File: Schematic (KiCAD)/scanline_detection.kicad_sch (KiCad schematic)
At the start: 95 parts, among them M2 NOR_2, M3 BIGBUF, X12 D-FF Reset, X13 NAND_2, X14 BUFFER, X16 INVERT, X17 NAND_2, X26 INVERT, X27 D-FF No Reset, X28 INVERT, X4 NAND_2, X5 D-FF No Reset, X6 NAND_4, X7 INVERT, X8 Reg 2 DFF-No-Reset N, X9 NAND_2, Y1 BUFFER, Y10 XNOR_2, Y13 XNOR_2, Y15 NOR_2, Y17 XNOR_2, Y2,7,9,14,16,21,23,28 Reg 8 D-Latch, Y20 XNOR_2, Y22 NAND_4, Y24 XNOR_2, Y27 XNOR_2, Y29 NOR_2, Y3 XNOR_2, Y30 INVERT, Y31 D-FF Reset, Y32 INVERT, Y6 XNOR_2, Y8 NAND_4

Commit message: - Lots of additional comments and signal name improvements.  - "Don't know what this is yet but it is important" section of the pulse channels:    - I worked out the logic and it is a 4-bit binary up-counter with preload, made from gates and D-latches instead of T-flip-flops.    - It is extremely similar to the envelope counter, but takes twice the die space and much more traces.    - None of its outputs go anywhere else, so I believe that it has no actual function.    - It seems to be a previous attempt at making the envelope counter and it got disconnected and left in.    - Each pulse channel has its own copy and I moved both of them to the "Artifacts" sheet.    - The wasted space amounts to about half of one of the large columns on the left side of the die.  - A couple of "OAI2" cells that noted "unclear order": I determined the correct order of the inputs based on several others which were known.  - Deduced the purpose of the 2 separate methods of scanline detection:    - The one looking for 3 consecutive reads finds the start of a scanline.    - The one counting PPU /RD to find PPU cycle 336, finds the end of the scanline.    - I moved these beside each other on the same sheet for clarity.  - A66.5 Changed from Nand to Nor in order to make sense.  - Basic test mode:    - Pin 92: Active low, enables test mode.    - Pin 29: In test mode, it gives external control of "Scanline Start Detection", which is normally done with the familiar 3 matching PPU reads.  When not in test mode, the pin has no function.    - Pin 30: In test mode, it gives external control of "Scanline End Detection", which is normally done by counting PPU /RD to find PPU cycle 336.  It also gives control of "Pulse Length Clock" when in test mode.  When not in test mode, the pin has no function.    - Pin 98/SL3: In test mode, it gives external control of "Pulse Timer Clock".  Whether or not in test mode, this pin low makes the MMC5 pretend $5104 had not yet been written since reset, probably as a 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
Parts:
- added P3, P4, R7, R8: INVERT, symbol MMC5:INVERT
- added R1: AOI_2, symbol MMC5:AOI_2
- added R6: NAND_2, symbol MMC5:NAND_2
- added T5: BUFFER, symbol MMC5:BUFFER
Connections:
- net External_Scanline_Input_PIN_29 is gone; now on net /Test_Input_PIN_29{PinInv}: AA4. (X)
- net at X7. (X): now also Z23. (/Q); no longer X6. (X)
- net at X13. (X): now also X12. (/Q); no longer X14. (X)
- net at X9. (X): now also Z24. (X); no longer X8. (/Q1)
- net at AA10. (X): now also AA13. (X); no longer AA9. (X)
- net at AA16. (X): now also AA14. (X); no longer AA17. (X)
- net at Z2-Z18. (/Q7): now also Y3. (X); no longer Z19. (X)
- net at Y29. (X): now also Y31. (/Q); no longer Y30. (X)
- net at Y15. (X): now also Y22. (X); no longer Y29. (X)
- net /Scanline_Start_Detected{AA3}: now reaches Y31. (/Q)
- net /Scanline_Start_Detected{AA3}: now also AA3. (X), R2. (X), Z1. (X), Z23. (/Q); no longer Y29. (X)
- net at Y17. (X): now also Y22. (X); no longer Y2,7,9,14,16,21,23,28. (Q7)
- net at Y24. (X): now also Y22. (X); no longer Y2,7,9,14,16,21,23,28. (Q7)
- net at Y20. (X): now also Y22. (X); no longer Y2,7,9,14,16,21,23,28. (Q7)
- net at Y6. (X): now also Y8. (X); no longer Y2,7,9,14,16,21,23,28. (Q7)
- net at Y13. (X): now also Y8. (X); no longer Y2,7,9,14,16,21,23,28. (Q7)
- net at Y10. (X): now also Y8. (X); no longer Y2,7,9,14,16,21,23,28. (Q7)
- net at Y3. (X): now also Y8. (X); no longer Y2,7,9,14,16,21,23,28. (Q7)
- net at Y27. (X): now also Y22. (X); no longer Y2,7,9,14,16,21,23,28. (Q7)
- net at AA20. (X): now also AA16. (X); no longer AA21. (X)
- net at AA19. (X): now also AB18. (X); no longer AA22. (X)
- net at AA15. (X): now also AB17. (X); no longer AA11. (X)
- net at X17. (X): now also Z20. (X); no longer X26. (X)
- net at Y8. (X): now also Y15. (X); no longer Y6. (X)
- net at AA5. (X): now also AA15. (X); no longer AA10. (X)
- net at AA2. (X): now also AB1. (X); no longer AA3. (X)
- net /Test_Input_PIN_29{PinInv}: now reaches AA4. (X)
- net /Test_Input_PIN_29{PinInv}: no longer AA2. (X)
- net at AB1. (X): now also AB2(a). (X); no longer AA2. (X)
- net at N39. (X): now also N38. (X); no longer M2. (X)
- net +Use_Internal_Scanline_Detection_PIN_92 renamed +Test_Mode_PIN_92{PinInv}
- removed net +Use_Internal_Scanline_Detection{AA1}: AA1. (X), AA2. (X)
- removed net /New_Scanline_Detected{AA3}: AA3. (X), R2. (X), Y31. (/Q), Z1. (X), Z23. (/Q)
- net /New_Scanline_Detected{R2} renamed /Scanline_Start_Detected{R2}
- removed net /Use_Internal_Scanline_Detection{AA1}: AA1. (X), AA2. (X)
- new net: X4. (X), X5. (/Q)
- new net: X16. (X), X4. (X)
- new net: X5. (/Q), X6. (X)
- new net: X6. (X), X7. (X)
- new net: X13. (X), X14. (X)
- new net: X13. (X), Y31. (/Q), Y32. (X)
- new net: P4. (X), R1. (X)
- new net: AA1. (X), AA2. (X), R1. (X) (x2)
- new net: P3. (X), R1. (X)
- new net: X8. (/Q1), X9. (X) (x2)
- new net: AA9. (X), AB6. (/Q)
- new net: AA10. (X), AA9. (X)
- new net: AA17. (X), AB16. (/Q)
- new net: AA16. (X), AA17. (X)
- new net: Z19. (X), Z2-Z18. (/Q7)
- new net: R6. (X), R7. (X)
- new net: Y29. (X), Y30. (X)
- new net: Y15. (X), Y29. (X)
- new net: Y1. (X), Y2,7,9,14,16,21,23,28. (Q7)
- new net: Y17. (X), Y2,7,9,14,16,21,23,28. (Q7)
- new net: Y2,7,9,14,16,21,23,28. (Q7), Y24. (X)
- new net: Y2,7,9,14,16,21,23,28. (Q7), Y20. (X)
- new net: Y2,7,9,14,16,21,23,28. (Q7), Y6. (X)
- new net: Y13. (X), Y2,7,9,14,16,21,23,28. (Q7)
- new net: Y10. (X), Y2,7,9,14,16,21,23,28. (Q7)
- new net: Y2,7,9,14,16,21,23,28. (Q7), Y3. (X)
- new net: Y2,7,9,14,16,21,23,28. (Q7), Y27. (X)
- new net: AA20. (X), AA21. (X)
- new net: AA21. (X), AB22. (/Q)
- new net: AA7. (X), AB10. (/Q), AB13. (/Q), AB16. (/Q), AB19. (/Q), AB22. (/Q), AB6. (/Q), AB7. (/Q)
- new net: AB3. (X), AC12. (/Q), AC15. (/Q), AC18. (/Q), AC21. (/Q), AC24. (/Q), AC27. (/Q), AC9. (/Q)
- new net: AB11. (X), AC15. (/Q)
- new net: AA12. (X), AB7. (/Q)
- new net: Y17. (X), Z2-Z18. (/Q7), Z22. (X)
- new net: Y24. (X), Z2-Z18. (/Q7), Z22. (X)
- new net: Y20. (X), Z2-Z18. (/Q7), Z22. (X)
- new net: Y27. (X), Z2-Z18. (/Q7), Z22. (X)
- new net: Y6. (X), Z2-Z18. (/Q7)
- new net: Y13. (X), Z2-Z18. (/Q7)
- new net: Y10. (X), Z2-Z18. (/Q7)
- new net: Z1. (X), Z2-Z18. (/Q7)
- new net: AA10. (X), AA12. (X)
- new net: AA22. (X), AC27. (/Q)
- new net: AA11. (X), AC12. (/Q)
- new net: AC2. (Q1), AC6. (X) (x2)
- new net: AA19. (X), AA22. (X)
- new net: AA11. (X), AA15. (X)
- new net: AA18. (X), AB19. (/Q)
- new net: AA16. (X), AA18. (X)
- new net: X17. (X), X26. (X)
- new net: M2. (X), X17. (X)
- new net: AA10. (X), AA5. (X)
- new net: AA5. (X), AB2. (Q2)
- new net: AA19. (X), AA5. (X)
- new net: AA16. (X), AA5. (X)
- new net: AA10. (X), AA8. (X)
- new net: AA2. (X), AA3. (X)
- new net: AA2. (X), AA4. (X)
- new net: Z24. (X), Z25. (X)
- new net: AA8. (X), AC9. (/Q)
- new net: M3. (X), N38. (X)
- new net: AB1. (X), AB2. (Q2) (x3)
- new net: M2. (X), N39. (X)
- new net: AA13. (X), AB10. (/Q)
- new net: AB17. (X), AC21. (/Q)
- new net: N16. (X), N9. (X)
- new net: AA15. (X), AB12. (X)
- new net: AB12. (X), AC18. (/Q)
- new net: R7. (X), R8. (X)
- new net: X27. (/Q), X28. (X)
- new net: AB18. (X), AC24. (/Q)
- new net: AA14. (X), AB13. (/Q)
- new net: AA15. (X), AB11. (X)
- new net +PPU_Cycle_336{R4}: R6. (X)
- new net Increment_Scanline_Fetch_Count{S6}: R6. (X)
- new net Scanline_End_Detected_Internal{R8}: R1. (X), R8. (X)
- new net Scanline_End_Detected{P3}: P3. (X), T5. (X)
- new net Scanline_End_Detected{T5}: T5. (X)
- new net /Test_Input_PIN_30{PinInv}: P4. (X)
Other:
- note added: "+Use External Scanline Detection"
- note added: "+Use Internal Scanline Detection"
- note added: "External Scanline End"
- note added: "External Scanline Start"
- note added: "Scanline End Detection"
- note added: "Scanline Start Detection"
- moved on the sheet: AA1, AA10, AA11, AA12, AA13, AA14, AA15, AA16, AA17, AA18, AA19, AA2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

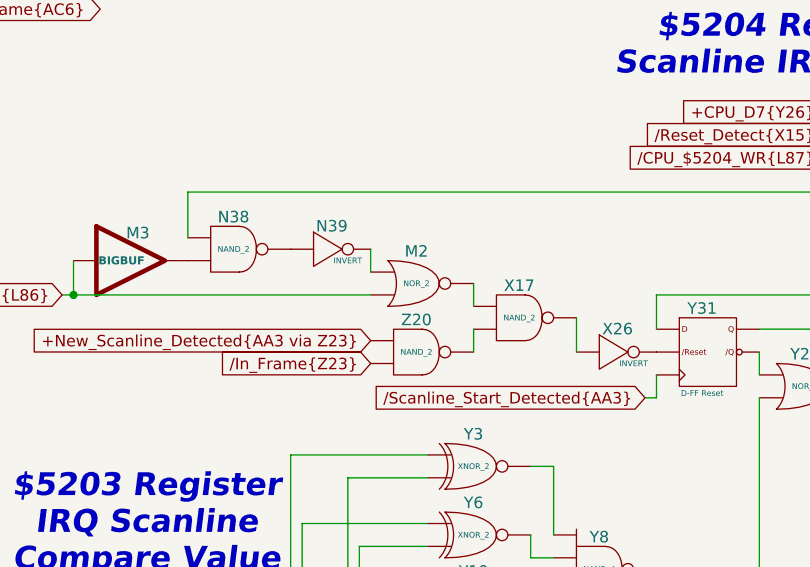
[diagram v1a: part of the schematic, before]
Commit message: I fixed 2 errors in the letterless MMC5 tracing:
1. BK5 is a NAND-4 gate.  It was thought to be NAND-3 before.
2.  BL83 and BL96 signals got swapped here before.  They actually cross each other:

BL83 = "PPU_RW_Mode_%0x_Access"
BL96 = "+ExRAM_Mode_$0x"

This propagated out to several changes in the schematic.
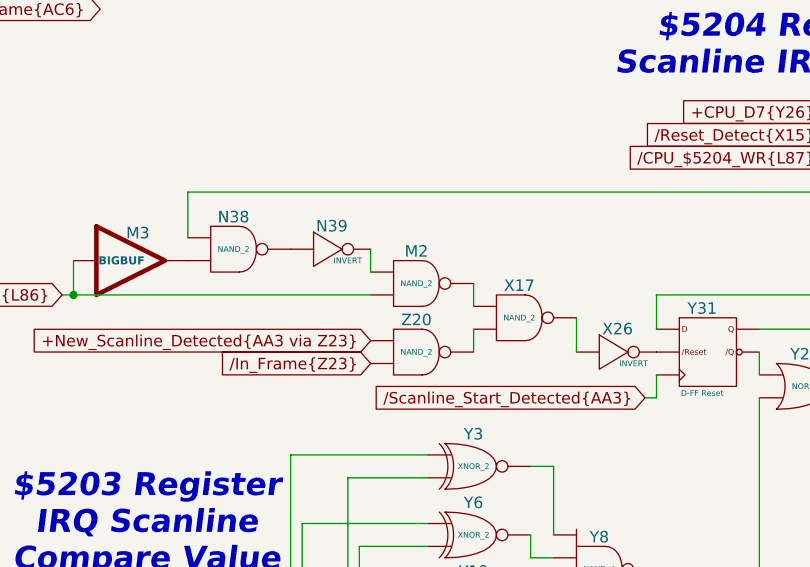
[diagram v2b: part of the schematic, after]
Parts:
- removed M2: NOR_2, symbol MMC5:NOR_2
- added M2: NAND_2, symbol MMC5:NAND_2
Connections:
- net /CPU_$5204_RD{L86}: now also M2. (X)
- net at X7. (X): now also Z23. (/Q); no longer X6. (X)
- net at X13. (X): now also X12. (/Q); no longer X14. (X)
- net at X9. (X): now also Z24. (X); no longer X8. (/Q1)
- net at AA10. (X): now also AA13. (X); no longer AA9. (X)
- net at AA16. (X): now also AA14. (X); no longer AA17. (X)
- net at Z2-Z18. (/Q7): now also Y3. (X); no longer Z19. (X)
- net at R7. (X): now also R8. (X); no longer R6. (X)
- net at Y29. (X): now also Y31. (/Q); no longer Y30. (X)
- net at Y15. (X): now also Y22. (X); no longer Y29. (X)
- net at Y17. (X): now also Y22. (X); no longer Y2,7,9,14,16,21,23,28. (Q7)
- net at Y24. (X): now also Y22. (X); no longer Y2,7,9,14,16,21,23,28. (Q7)
- net at Y20. (X): now also Y22. (X); no longer Y2,7,9,14,16,21,23,28. (Q7)
- net at Y6. (X): now also Y8. (X); no longer Y2,7,9,14,16,21,23,28. (Q7)
- net at Y13. (X): now also Y8. (X); no longer Y2,7,9,14,16,21,23,28. (Q7)
- net at Y10. (X): now also Y8. (X); no longer Y2,7,9,14,16,21,23,28. (Q7)
- net at Y3. (X): now also Y8. (X); no longer Y2,7,9,14,16,21,23,28. (Q7)
- net at Y27. (X): now also Y22. (X); no longer Y2,7,9,14,16,21,23,28. (Q7)
- net at AA20. (X): now also AA16. (X); no longer AA21. (X)
- net at AA19. (X): now also AB18. (X); no longer AA22. (X)
- net at AA15. (X): now also AB17. (X); no longer AA11. (X)
- net at X17. (X): now also Z20. (X); no longer X26. (X)
- net at Y8. (X): now also Y15. (X); no longer Y6. (X)
- net at AA5. (X): now also AA15. (X); no longer AA10. (X)
- net at AA2. (X): now also AB1. (X); no longer AA3. (X)
- net at AB1. (X): now also AB2(a). (X); no longer AA2. (X)
- net at N39. (X): now also N38. (X)
- new net: X4. (X), X5. (/Q)
- new net: X16. (X), X4. (X)
- new net: X5. (/Q), X6. (X)
- new net: X6. (X), X7. (X)
- new net: X13. (X), X14. (X)
- new net: X13. (X), Y31. (/Q), Y32. (X)
- new net: P4. (X), R1. (X)
- new net: AA1. (X), AA2. (X), R1. (X) (x2)
- new net: P3. (X), R1. (X)
- new net: X8. (/Q1), X9. (X) (x2)
- new net: AA9. (X), AB6. (/Q)
- new net: AA10. (X), AA9. (X)
- new net: AA17. (X), AB16. (/Q)
- new net: AA16. (X), AA17. (X)
- new net: Z19. (X), Z2-Z18. (/Q7)
- new net: R6. (X), R7. (X)
- new net: Y29. (X), Y30. (X)
- new net: Y15. (X), Y29. (X)
- new net: Y1. (X), Y2,7,9,14,16,21,23,28. (Q7)
- new net: Y17. (X), Y2,7,9,14,16,21,23,28. (Q7)
- new net: Y2,7,9,14,16,21,23,28. (Q7), Y24. (X)
- new net: Y2,7,9,14,16,21,23,28. (Q7), Y20. (X)
- new net: Y2,7,9,14,16,21,23,28. (Q7), Y6. (X)
- new net: Y13. (X), Y2,7,9,14,16,21,23,28. (Q7)
- new net: Y10. (X), Y2,7,9,14,16,21,23,28. (Q7)
- new net: Y2,7,9,14,16,21,23,28. (Q7), Y3. (X)
- new net: Y2,7,9,14,16,21,23,28. (Q7), Y27. (X)
- new net: AA20. (X), AA21. (X)
- new net: AA21. (X), AB22. (/Q)
- new net: AA7. (X), AB10. (/Q), AB13. (/Q), AB16. (/Q), AB19. (/Q), AB22. (/Q), AB6. (/Q), AB7. (/Q)
- new net: AB3. (X), AC12. (/Q), AC15. (/Q), AC18. (/Q), AC21. (/Q), AC24. (/Q), AC27. (/Q), AC9. (/Q)
- new net: AB11. (X), AC15. (/Q)
- new net: AA12. (X), AB7. (/Q)
- new net: M2. (X), X17. (X)
- new net: M2. (X), N39. (X)
- new net: Y17. (X), Z2-Z18. (/Q7), Z22. (X)
- new net: Y24. (X), Z2-Z18. (/Q7), Z22. (X)
- new net: Y20. (X), Z2-Z18. (/Q7), Z22. (X)
- new net: Y27. (X), Z2-Z18. (/Q7), Z22. (X)
- new net: Y6. (X), Z2-Z18. (/Q7)
- new net: Y13. (X), Z2-Z18. (/Q7)
- new net: Y10. (X), Z2-Z18. (/Q7)
- new net: Z1. (X), Z2-Z18. (/Q7)
- new net: AA10. (X), AA12. (X)
- new net: AA22. (X), AC27. (/Q)
- new net: AA11. (X), AC12. (/Q)
- new net: AC2. (Q1), AC6. (X) (x2)
- new net: AA19. (X), AA22. (X)
- new net: AA11. (X), AA15. (X)
- new net: AA18. (X), AB19. (/Q)
- new net: AA16. (X), AA18. (X)
- new net: X17. (X), X26. (X)
- new net: AA10. (X), AA5. (X)
- new net: AA5. (X), AB2. (Q2)
- new net: AA19. (X), AA5. (X)
- new net: AA16. (X), AA5. (X)
- new net: AA10. (X), AA8. (X)
- new net: AA2. (X), AA3. (X)
- new net: AA2. (X), AA4. (X)
- new net: Z24. (X), Z25. (X)
- new net: AA8. (X), AC9. (/Q)
- new net: M3. (X), N38. (X)
- new net: AB1. (X), AB2. (Q2) (x3)
- new net: AA13. (X), AB10. (/Q)
- new net: AB17. (X), AC21. (/Q)
- new net: N16. (X), N9. (X)
- new net: AA15. (X), AB12. (X)
- new net: AB12. (X), AC18. (/Q)
- new net: X27. (/Q), X28. (X)
- new net: AB18. (X), AC24. (/Q)
- new net: AA14. (X), AB13. (/Q)
- new net: AA15. (X), AB11. (X)
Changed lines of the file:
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@@
+	)
+	(symbol
+		(lib_name "NAND_2_12")
+		(lib_id "MMC5:NAND_2")
+		(at 242.57 105.41 0)
+		(unit 1)
+		(exclude_from_sim no)
+		(in_bom yes)
+		(on_board yes)
+		(dnp no)
+		(fields_autoplaced yes)
+		(property "Reference" "M2"
+			(at 242.57 101.092 0)
+			(do_not_autoplace yes)
+			(effects
+				(font
+					(size 1.27 1.27)
+				)
+				(justify top)
+			)
+		)
+		(property "Value" "NAND_2"
+			(at 242.57 105.41 0)
+			(do_not_autoplace yes)
+			(effects
+				(font
+					(size 0.635 0.635)
+				)
+			)
+		)
+		(property "Footprint" ""
+			(at 242.57 105.41 0)
+			(effects
+				(font
+					(size 1.27 1.27)
+				)
+				(hide yes)
+			)
+		)
+		(property "Datasheet" ""
+			(at 242.57 105.41 0)
+			(effects
+				(font
+					(size 1.27 1.27)
+				)
+				(hide yes)
+			)
+		)
+		(property "Description" ""
+			(at 242.57 105.41 0)
+			(effects
+				(font
+					(size 1.27 1.27)
+				)
+				(hide yes)
+			)
+		)
+		(pin ""
+		)
+		(pin ""
+		)
+		(pin ""
+		)
+		(instances
+			(project "MMC5"
+				(path "/46093bf6-f83e-4237-9ece-7350a682aff0/6046dae0-7343-4130-8be0-3bf9e6fb16fb"
+					(reference "M2")
+					(unit 1)
+				)
+			)
+		)
 	)
 	(symbol
@@
 					(unit 1)
 				)
-			)
-		)
-	)
-	(symbol
-		(lib_name "NOR_2_2")
-		(lib_id "MMC5:NOR_2")
-		(at 242.57 105.41 0)
-		(unit 1)
-		(exclude_from_sim no)
-		(in_bom yes)
-		(on_board yes)
-		(dnp no)
-		(fields_autoplaced yes)
-		(property "Reference" "M2"
-			(at 242.57 101.092 0)
-			(do_not_autoplace yes)
-			(effects
-				(font
-					(size 1.27 1.27)
-				)
-				(justify top)
-			)
-		)
-		(property "Value" "NOR_2"
-			(at 242.57 105.41 0)
-			(do_not_autoplace yes)
-			(effects
-				(font
-					(size 0.635 0.635)
-				)
-			)
-		)
-		(property "Footprint" ""
-			(at 242.57 105.41 0)
-			(effects
-				(font
-					(size 1.27 1.27)
-				)
-				(hide yes)
-			)
-		)
-		(property "Datasheet" ""
-			(at 242.57 105.41 0)
-			(effects
-				(font
-					(size 1.27 1.27)
-				)
-				(hide yes)
-			)
-		)
-		(property "Description" ""
-			(at 242.57 105.41 0)
-			(effects
-				(font
-					(size 1.27 1.27)
-				)
-				(hide yes)
-			)
-		)
-		(pin ""
-		)
-		(pin ""
-		)
-		(pin ""
-		)
-		(instances
-			(project ""
-				(path "/46093bf6-f83e-4237-9ece-7350a682aff0/6046dae0-7343-4130-8be0-3bf9e6fb16fb"
-					(reference "M2")
-					(unit 1)
-				)
